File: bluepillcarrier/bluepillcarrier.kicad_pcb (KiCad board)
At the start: 4 copper layers, 81.3 x 86.4 mm, 118 parts, among them CN1 USB, CN2 Can, CN3 Can, CN4 RTC, CN5 RS485, CN6 485, CN7 BME, CN8 SWD, Q1 SS8050, SW1 Usr1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

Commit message: Some updates and fixes
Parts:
- added JP3: USB pwr, Connector_PinHeader_2.54mm:PinHeader_1x02_P2.54mm_Vertical, F.Cu at (180.4, 96.2)
- added kibuzzard-6942718F: G***, kibuzzard-6942718F, F.Cu at (183.0, 96.2)
- added kibuzzard-69427268: G***, kibuzzard-69427268, F.Cu at (147.9, 99.3)
- added kibuzzard-69427281: G***, kibuzzard-69427281, F.Cu at (182.0, 103.5)
- added kibuzzard-694272A7: G***, kibuzzard-694272A7, F.Cu at (180.4, 84.7)
- added kibuzzard-694272CE: G***, kibuzzard-694272CE, F.Cu at (157.8, 41.9)
- added kibuzzard-6942731B: G***, kibuzzard-6942731B, F.Cu at (121.9, 97.0)
- added kibuzzard-69427335: G***, kibuzzard-69427335, F.Cu at (184.8, 88.9)
- moved kibuzzard-69415277 9.89 mm to (190.5, 112.2), turned to 0 degrees
- moved kibuzzard-69415288 7.44 mm to (190.5, 89.5), turned to 0 degrees
- moved C1 7.03 mm to (175.0, 103.8)
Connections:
- C3 pad 1: /3V3 -> /5V
- D1 pad 1: /5V -> Net-(D1-K)
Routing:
- net Net-(D1-K): track 0.00 -> 14.8 mm
- net /5V: track 158.2 -> 148.1 mm, vias 3 -> 4
- net /RX3: track 113.7 -> 119.6 mm
- net /TX3: track 111.1 -> 116.7 mm
- net /3V3: track 303.5 -> 306.9 mm
- net GND: vias 122 -> 121

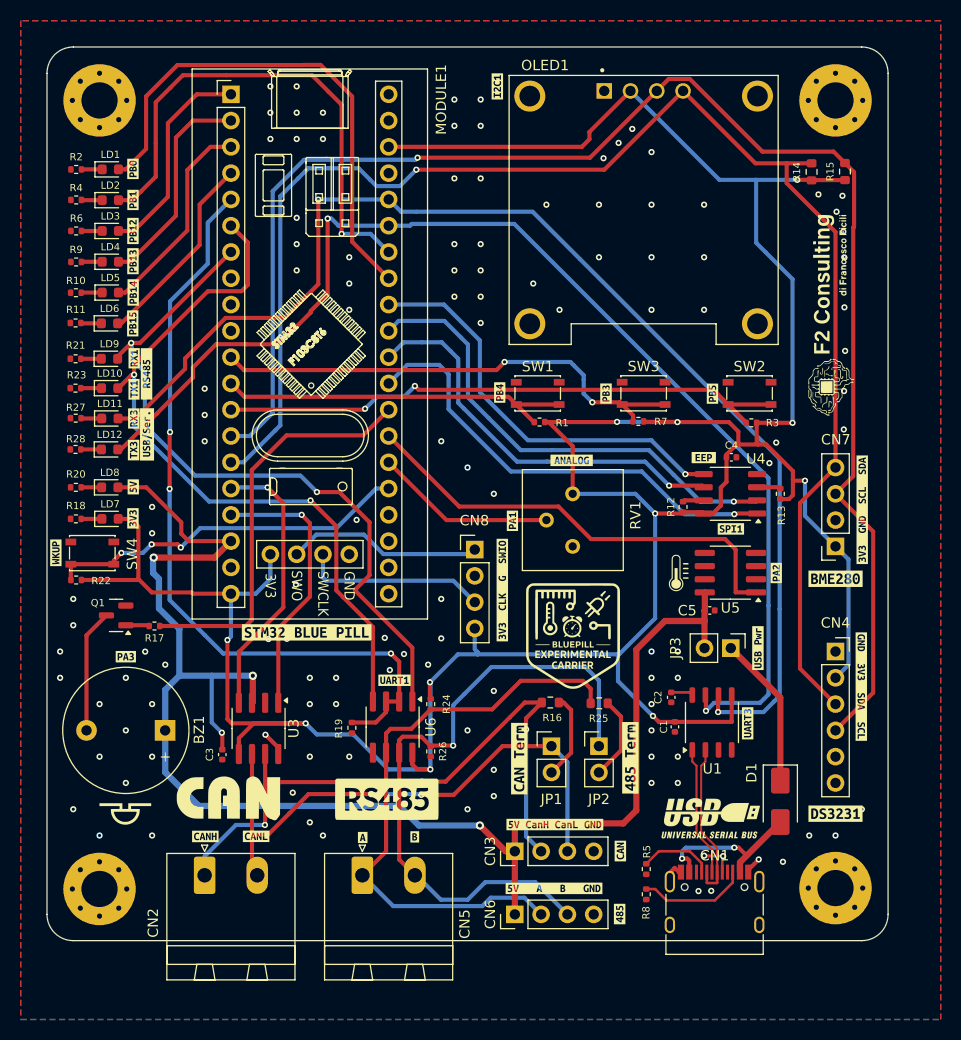
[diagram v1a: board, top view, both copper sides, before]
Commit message: Fixes: - Corrected OLED footprint - Green led resistor set to 1k - Updated all the labels to 1mm for better visibility - Moved trimmer a bit below to save a bit of space for buttons
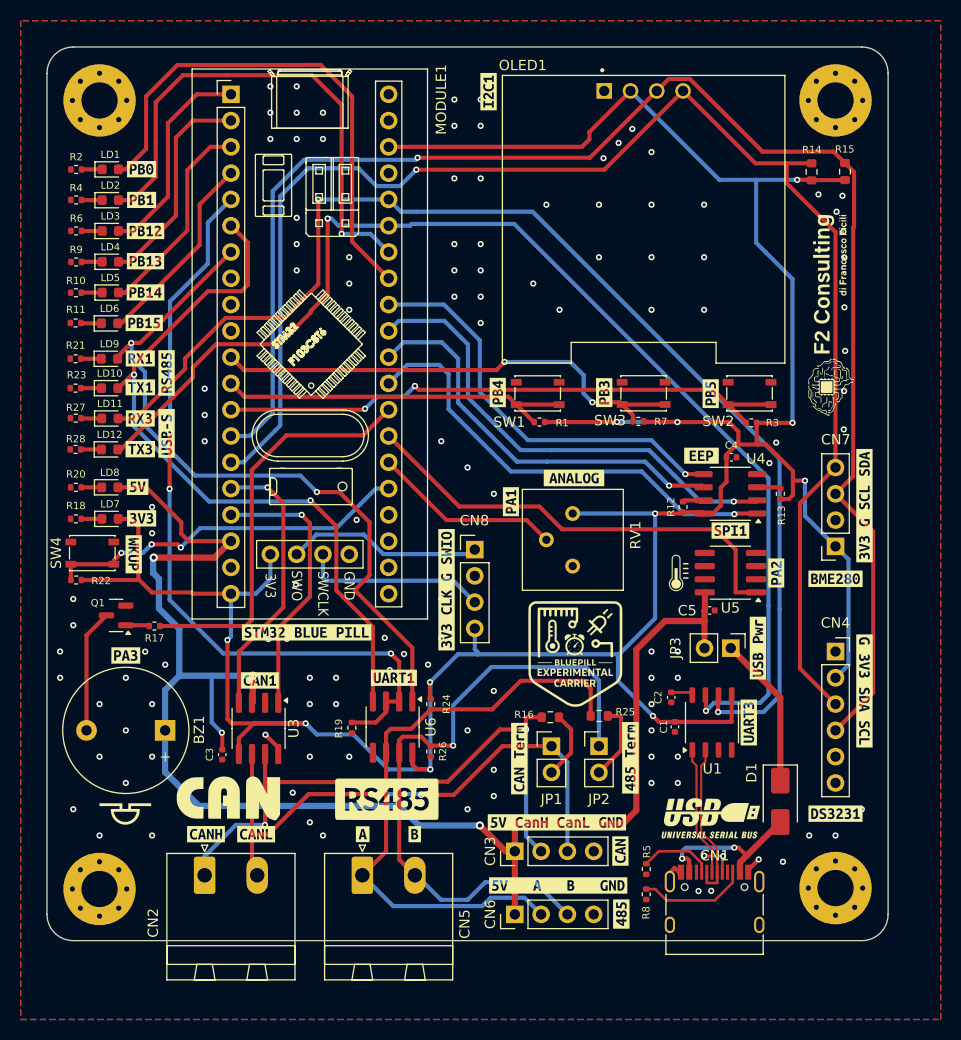
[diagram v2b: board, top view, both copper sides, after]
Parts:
- removed kibuzzard-69415046: G***, kibuzzard-69415046
- removed kibuzzard-69415055: G***, kibuzzard-69415055
- removed kibuzzard-6941506E: G***, kibuzzard-6941506E
- removed kibuzzard-6941507C: G***, kibuzzard-6941507C
- removed kibuzzard-6941519E: G***, kibuzzard-6941519E
- removed kibuzzard-694151C2: G***, kibuzzard-694151C2
- removed kibuzzard-694151C8: G***, kibuzzard-694151C8
- removed kibuzzard-694151D0: G***, kibuzzard-694151D0
- removed kibuzzard-694151D6: G***, kibuzzard-694151D6
- removed kibuzzard-694151DF: G***, kibuzzard-694151DF
- removed kibuzzard-694151EC: G***, kibuzzard-694151EC
- removed kibuzzard-69415200: G***, kibuzzard-69415200
- removed kibuzzard-69415214: G***, kibuzzard-69415214
- removed kibuzzard-69415225: G***, kibuzzard-69415225
- removed kibuzzard-69415240: G***, kibuzzard-69415240
- removed kibuzzard-69415302: G***, kibuzzard-69415302
- removed kibuzzard-6941532E: G***, kibuzzard-6941532E
- removed kibuzzard-6941537C: G***, kibuzzard-6941537C
- removed kibuzzard-694153D2: G***, kibuzzard-694153D2
- removed kibuzzard-694153F7: G***, kibuzzard-694153F7
- removed kibuzzard-69415541: G***, kibuzzard-69415541
- removed kibuzzard-6941554B: G***, kibuzzard-6941554B
- removed kibuzzard-6941601C: G***, kibuzzard-6941601C
- removed kibuzzard-6941604D: G***, kibuzzard-6941604D
- removed kibuzzard-69416060: G***, kibuzzard-69416060
- removed kibuzzard-69416065: G***, kibuzzard-69416065
- removed kibuzzard-694160D3: G***, kibuzzard-694160D3
- removed kibuzzard-69416122: G***, kibuzzard-69416122
- removed kibuzzard-69416261: G***, kibuzzard-69416261
- removed kibuzzard-69416274: G***, kibuzzard-69416274
- removed kibuzzard-694165FB: G***, kibuzzard-694165FB
- removed kibuzzard-69416679: G***, kibuzzard-69416679
- removed kibuzzard-69416686: G***, kibuzzard-69416686
- removed kibuzzard-6942718F: G***, kibuzzard-6942718F
- removed kibuzzard-69427268: G***, kibuzzard-69427268
- removed kibuzzard-69427281: G***, kibuzzard-69427281
- removed kibuzzard-694272A7: G***, kibuzzard-694272A7
- removed kibuzzard-694272CE: G***, kibuzzard-694272CE
- removed kibuzzard-6942731B: G***, kibuzzard-6942731B
- removed kibuzzard-69427335: G***, kibuzzard-69427335
- added kibuzzard-69594BD1: G***, kibuzzard-69594BD1, F.Cu at (123.4, 49.9)
- added kibuzzard-69594BE1: G***, kibuzzard-69594BE1, F.Cu at (123.4, 52.9)
- added kibuzzard-69594BEF: G***, kibuzzard-69594BEF, F.Cu at (123.8, 55.9)
- added kibuzzard-69594BFB: G***, kibuzzard-69594BFB, F.Cu at (123.8, 58.8)
- added kibuzzard-69594C11: G***, kibuzzard-69594C11, F.Cu at (123.8, 61.8)
- added kibuzzard-69594C18: G***, kibuzzard-69594C18, F.Cu at (123.7, 64.8)
- added kibuzzard-69594C37: G***, kibuzzard-69594C37, F.Cu at (123.3, 68.2)
- added kibuzzard-69594C3C: G***, kibuzzard-69594C3C, F.Cu at (123.3, 71.0)
- added kibuzzard-69594C59: G***, kibuzzard-69594C59, F.Cu at (125.9, 69.6)
- added kibuzzard-69594C68: G***, kibuzzard-69594C68, F.Cu at (123.3, 74.0)
- added kibuzzard-69594C6D: G***, kibuzzard-69594C6D, F.Cu at (123.3, 77.0)
- added kibuzzard-69594C8A: G***, kibuzzard-69594C8A, F.Cu at (123.1, 80.6)
- added kibuzzard-69594C8F: G***, kibuzzard-69594C8F, F.Cu at (123.4, 83.7)
- added kibuzzard-69594C94: G***, kibuzzard-69594C94, F.Cu at (122.7, 87.1)
- added kibuzzard-69594CA2: G***, kibuzzard-69594CA2, F.Cu at (139.4, 94.7)
- added kibuzzard-69594CA9: G***, kibuzzard-69594CA9, F.Cu at (129.7, 114.2)
- added kibuzzard-69594CAE: G***, kibuzzard-69594CAE, F.Cu at (134.5, 114.2)
- added kibuzzard-69594CB5: G***, kibuzzard-69594CB5, F.Cu at (144.8, 114.2)
- added kibuzzard-69594CD1: G***, kibuzzard-69594CD1, F.Cu at (149.8, 114.2)
- added kibuzzard-69594CE1: G***, kibuzzard-69594CE1, F.Cu at (169.7, 115.8)
- added kibuzzard-69594CE6: G***, kibuzzard-69594CE6, F.Cu at (169.8, 121.9)
- added kibuzzard-69594CF8: G***, kibuzzard-69594CF8, F.Cu at (147.8, 99.1)
- added kibuzzard-69594D06: G***, kibuzzard-69594D06, F.Cu at (134.9, 99.3)
- added kibuzzard-69594D0E: G***, kibuzzard-69594D0E, F.Cu at (182.1, 103.4)
- added kibuzzard-69594D1B: G***, kibuzzard-69594D1B, F.Cu at (183.0, 96.2)
- added kibuzzard-69594D27: G***, kibuzzard-69594D27, F.Cu at (184.8, 88.9)
- added kibuzzard-69594D2D: G***, kibuzzard-69594D2D, F.Cu at (180.3, 84.8)
- added kibuzzard-69594D3A: G***, kibuzzard-69594D3A, F.Cu at (159.1, 82.0)
- added kibuzzard-69594D45: G***, kibuzzard-69594D45, F.Cu at (165.2, 79.8)
- added kibuzzard-69594D50: G***, kibuzzard-69594D50, F.Cu at (157.9, 71.5)
- added kibuzzard-69594D57: G***, kibuzzard-69594D57, F.Cu at (168.1, 71.5)
- added kibuzzard-69594D5C: G***, kibuzzard-69594D5C, F.Cu at (178.4, 71.6)
- added kibuzzard-69594D63: G***, kibuzzard-69594D63, F.Cu at (177.5, 77.6)
- added kibuzzard-69594D9E: G***, kibuzzard-69594D9E, F.Cu at (193.3, 82.4)
- added kibuzzard-69594DB5: G***, kibuzzard-69594DB5, F.Cu at (193.3, 100.3)
- added kibuzzard-69594DCB: G***, kibuzzard-69594DCB, F.Cu at (121.9, 96.9)
- added kibuzzard-69594DEB: G***, kibuzzard-69594DEB, F.Cu at (157.0, 42.4)
- added kibuzzard-69594DFC: G***, kibuzzard-69594DFC, F.Cu at (163.6, 113.0)
- added kibuzzard-69594E11: G***, kibuzzard-69594E11, F.Cu at (163.7, 119.1)
- added kibuzzard-69594E2D: G***, kibuzzard-69594E2D, F.Cu at (152.9, 90.6)
- added kibuzzard-69594E7B: G***, kibuzzard-69594E7B, F.Cu at (125.9, 75.4)
- JP1: value RS485 Term -> CAN Term
- R10, R11, R2, R21, R23, R27, R28, R4, R6, R9: value 330 -> 1k
- moved RV1 1.91 mm to (165.1, 83.2)
- moved G*** 1.75 mm to (165.4, 96.6)
- moved R16 1.42 mm to (162.9, 102.9)
- moved R25 1.22 mm to (167.7, 102.7)
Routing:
- net /3V3: track 306.9 -> 298.2 mm
- net /CANH: track 61.4 -> 58.2 mm
- net Net-(JP1-B): track 8.30 -> 6.61 mm
- net /A: track 57.8 -> 59.0 mm
- net /PA1: track 17.6 -> 18.3 mm
- net Net-(JP2-B): track 8.09 -> 7.59 mm

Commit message: Some additional fixes
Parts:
- removed U4: 25LCxxx, Package_SO:SO-8_3.9x4.9mm_P1.27mm
- removed kibuzzard-69594CF8: G***, kibuzzard-69594CF8
- removed kibuzzard-69594D0E: G***, kibuzzard-69594D0E
- added U2: M95512-WMN6TP, Package_SO:SOIC-8_3.9x4.9mm_P1.27mm, F.Cu at (180.5, 81.2)
- added kibuzzard-695AB373: G***, kibuzzard-695AB373, F.Cu at (182.1, 103.4)
- added kibuzzard-695AB37B: G***, kibuzzard-695AB37B, F.Cu at (147.8, 99.1)
- added kibuzzard-695AB3BA: G***, kibuzzard-695AB3BA, F.Cu at (115.5, 112.2)
- moved kibuzzard-69594C59 5.88 mm to (125.8, 75.5)
- moved kibuzzard-69594E7B 5.83 mm to (125.9, 69.6)
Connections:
- LD10 pad 2: /DI -> /TX1
- LD11 pad 2: /RX3 -> /RO
- LD12 pad 2: /TX3 -> /DI
- LD9 pad 2: /RO -> /RX1
- MODULE1 pad 35: /TX3 -> /DI
- MODULE1 pad 36: /RX3 -> /RO
- MODULE1 pad 6: /DI -> /TX1
- MODULE1 pad 7: /RO -> /RX1
- U1 pad 6: /RX3 -> /RX1
- U1 pad 7: /TX3 -> /TX1
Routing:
- net /RX3: track 119.6 -> 0.00 mm, vias 2 -> 0
- net /TX3: track 116.7 -> 0.00 mm, vias 2 -> 0
- net /RX1: track 0.00 -> 101.8 mm, vias 0 -> 2
- net /TX1: track 0.00 -> 99.9 mm, vias 0 -> 2
- net /RO: track 69.7 -> 89.5 mm, vias 2 -> 5
- net /DI: track 70.8 -> 82.1 mm, vias 2 -> 3
- net GND: track 6.48 -> 10.7 mm
- net /3V3: track 298.2 -> 298.9 mm, vias 11 -> 13

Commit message: some updates
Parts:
- removed kibuzzard-69594CA9: G***, kibuzzard-69594CA9
- removed kibuzzard-69594CAE: G***, kibuzzard-69594CAE
- removed kibuzzard-69594CB5: G***, kibuzzard-69594CB5
- removed kibuzzard-69594CD1: G***, kibuzzard-69594CD1
- added kibuzzard-69636EB7: G***, kibuzzard-69636EB7, F.Cu at (144.8, 113.9)
- added kibuzzard-69636ED7: G***, kibuzzard-69636ED7, F.Cu at (149.9, 113.9)
- added kibuzzard-69636EE0: G***, kibuzzard-69636EE0, F.Cu at (128.6, 113.8)
- added kibuzzard-69636EED: G***, kibuzzard-69636EED, F.Cu at (135.4, 113.8)
- OLED1: footprint oled:MODULE_DM-OLED096-636 -> bluepill:MODULE_DM-OLED096-636
- moved G*** 0.46 mm to (131.8, 110.2)
- moved G*** 0.38 mm to (147.2, 110.4)
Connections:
- LD10 pad 2: /TX1 -> /3V3
- LD11 pad 2: /RO -> /3V3
- LD12 pad 2: /DI -> /3V3
- LD9 pad 2: /RX1 -> /3V3
- R21 pad 2: GND -> /RX1
- R23 pad 2: GND -> /TX1
- R27 pad 2: GND -> /RO
- R28 pad 2: GND -> /DI
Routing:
- net /3V3: track 298.9 -> 315.6 mm, vias 13 -> 15
- net /DI: track 82.1 -> 88.7 mm, vias 3 -> 5
- net /RO: track 89.5 -> 95.6 mm, vias 5 -> 7
- net /TX1: track 99.9 -> 104.6 mm, vias 2 -> 3
- net /RX1: track 101.8 -> 106.4 mm

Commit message: - changed temperature sensor
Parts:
- removed U5: LM35-D, Package_SO:SOIC-8_3.9x4.9mm_P1.27mm
- removed kibuzzard-69594D27: G***, kibuzzard-69594D27
- added U4: TMP102xxDRL, Package_TO_SOT_SMD:SOT-563, F.Cu at (181.9, 88.9)
- added kibuzzard-69594DEB: G***, kibuzzard-69594DEB, F.Cu at (182.0, 92.0)
- moved C5 4.17 mm to (182.0, 90.6), turned to 180 degrees
- moved G*** 3.49 mm to (178.8, 88.7)
- moved kibuzzard-69594D1B 0.36 mm to (183.1, 96.5)
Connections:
- C5 pad 1: /5V -> /3V3
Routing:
- net /SCL1: track 148.5 -> 162.5 mm, vias 1 -> 3
- net /3V3: track 315.6 -> 328.3 mm, vias 15 -> 16
- net /PA2: track 44.2 -> 39.6 mm
- net /SDA1: track 145.3 -> 149.8 mm
- net GND: track 10.7 -> 14.0 mm
- net /5V: track 148.1 -> 145.3 mm
